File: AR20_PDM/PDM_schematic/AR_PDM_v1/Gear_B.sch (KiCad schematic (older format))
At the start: 18 parts, among them Q1 BTS50025-1TAD, U1 INA233

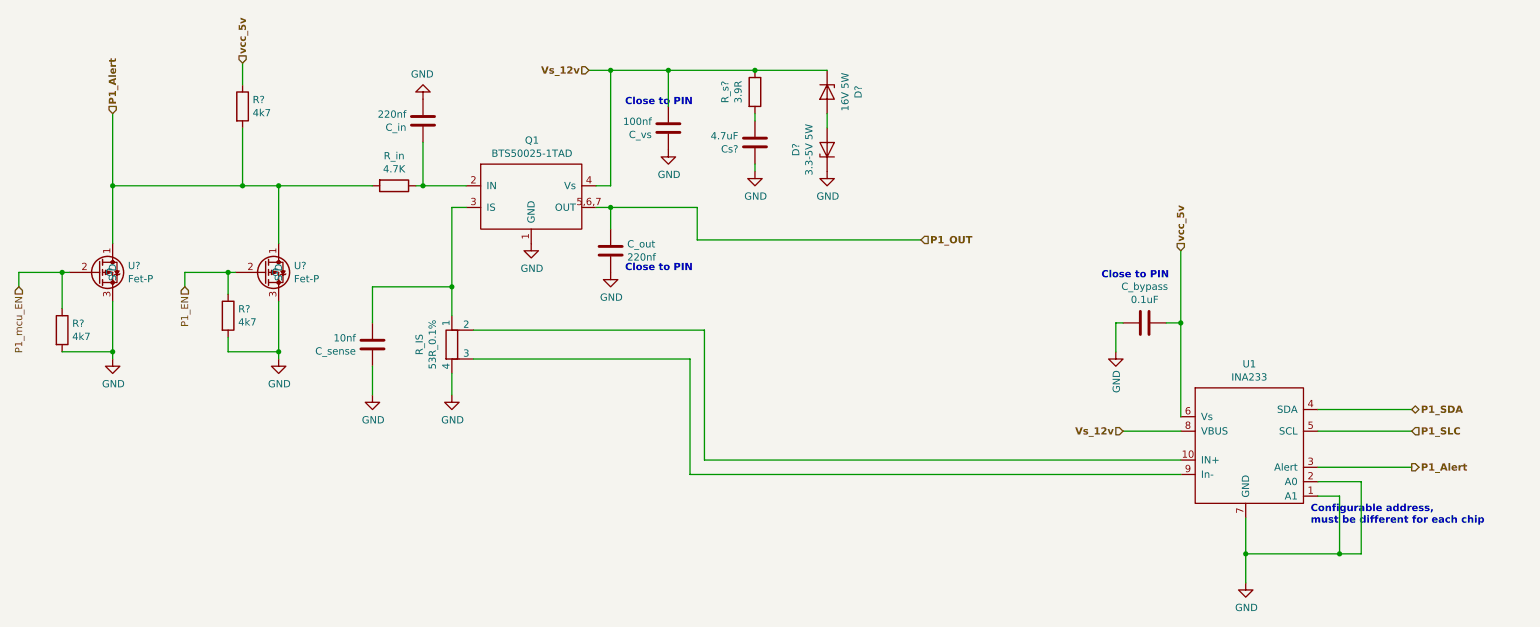
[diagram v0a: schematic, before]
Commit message: First draft of Gear phase, shutdown relays, and Direct phases.
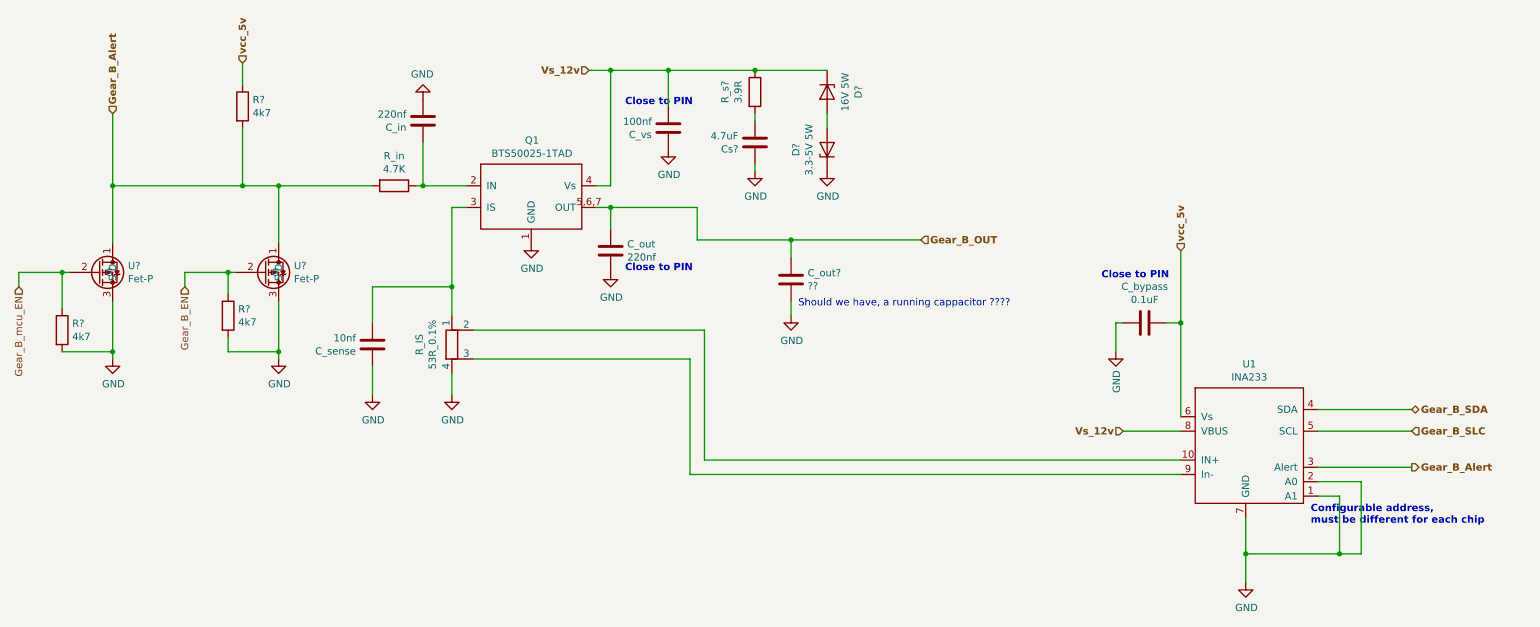
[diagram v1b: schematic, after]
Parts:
- added C_out?: ??, symbol AR20_PDM_v1-rescue:C-Device
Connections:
- net GND: now also C_out?.2
- net P1_Alert renamed Gear_B_Alert
- net P1_EN renamed Gear_B_EN
- net P1_OUT renamed Gear_B_OUT
- net Gear_B_OUT: now also C_out?.1
- net P1_SDA renamed Gear_B_SDA
- net P1_SLC renamed Gear_B_SLC
- net P1_mcu_EN renamed Gear_B_mcu_EN
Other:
- note added: "Should we have, a running cappacitor ????\n\n"
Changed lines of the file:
@@
 $Descr A4 11693 8268
 encoding utf-8
-Sheet 6 6
+Sheet 5 6
 Title ""
 Date ""
@@
 vcc_5v
 Text HLabel 10350 4350 2    50   Output ~ 10
-P1_Alert
+Gear_B_Alert
 Text HLabel 10350 3950 2    50   BiDi ~ 10
-P1_SDA
+Gear_B_SDA
 Text HLabel 10350 4100 2    50   Input ~ 10
-P1_SLC
+Gear_B_SLC
 Text Notes 4900 3000 0    50   ~ 10
 Close to PIN
@@
 	2250 1550 2250 1700
 Text HLabel 6950 2775 2    50   Input ~ 10
-P1_OUT
+Gear_B_OUT
 $Comp
 L AR20_PDM_v1-rescue:C-Device C_vs
@@
 	5350 3600 5350 4400
 Text HLabel 1350 1900 1    50   Input ~ 10
-P1_Alert
+Gear_B_Alert
 Wire Wire Line
 	9700 4350 10350 4350
@@
 Connection ~ 1000 3000
 Text HLabel 700  3100 3    50   Input ~ 0
-P1_mcu_EN
+Gear_B_mcu_EN
 Wire Wire Line
 	700  3000 700  3100
@@
 	1850 3100 1850 3000
 Text HLabel 1850 3100 3    50   Input ~ 0
-P1_EN
+Gear_B_EN
 Connection ~ 2150 3000
 Wire Wire Line
@@
 	5400 2550 5400 2775
 Wire Wire Line
-	5400 2775 6950 2775
+	5400 2775 6050 2775
 Connection ~ 4800 2550
 Wire Wire Line
@@
 Wire Wire Line
 	6300 1900 6300 2000
+$Comp
+L AR20_PDM_v1-rescue:C-Device C_out?
+U 1 1 5DEBB1FD
+P 6050 3050
+AR Path="/5DA89415/5DEBB1FD" Ref="C_out?"  Part="1"
+AR Path="/5DEB10A1/5DEBB1FD" Ref="Running_Cap?"  Part="1"
+AR Path="/5DEB20EA/5DEBB1FD" Ref="C_out?"  Part="1"
+F 0 "Running_Cap?" H 6165 3096 50  0000 L CNN
+F 1 "??" H 6165 3005 50  0000 L CNN
+F 2 "" H 6088 2900 50  0001 C CNN
+F 3 "~" H 6050 3050 50  0001 C CNN
+	1    6050 3050
+	1    0    0    -1
+$EndComp
+$Comp
+L AR20_PDM_v1-rescue:GND-power #PWR?
+U 1 1 5DEBC899
+P 6050 3300
+AR Path="/5DA89415/5DEBC899" Ref="#PWR?"  Part="1"
+AR Path="/5DEB10A1/5DEBC899" Ref="#PWR?"  Part="1"
+AR Path="/5DEB20EA/5DEBC899" Ref="#PWR?"  Part="1"
+F 0 "#PWR?" H 6050 3050 50  0001 C CNN
+F 1 "GND" H 6055 3127 50  0000 C CNN
+F 2 "" H 6050 3300 50  0001 C CNN
+F 3 "" H 6050 3300 50  0001 C CNN
+	1    6050 3300
+	1    0    0    -1
+$EndComp
+Wire Wire Line
+	6050 3300 6050 3200
+Wire Wire Line
+	6050 2900 6050 2775
+Connection ~ 6050 2775
+Wire Wire Line
+	6050 2775 6950 2775
+Text Notes 6100 3325 0    50   ~ 0
+Should we have, a running cappacitor ????\n\n
 $EndSCHEMATC

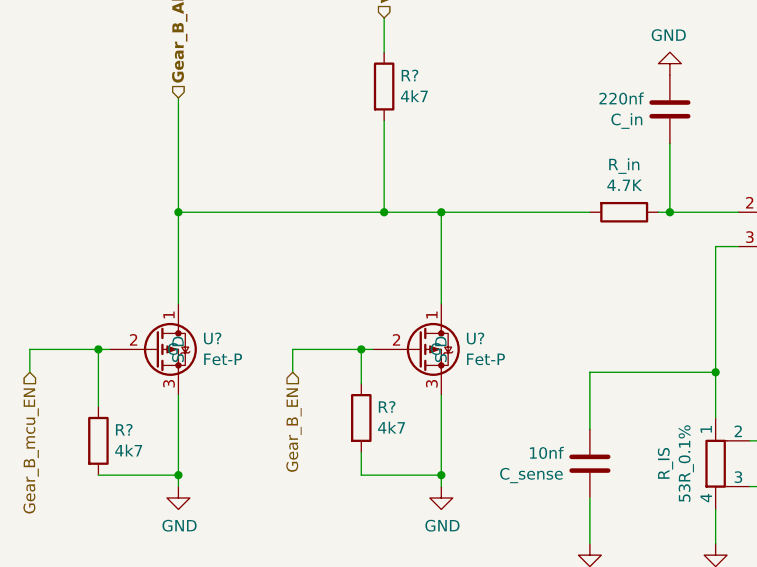
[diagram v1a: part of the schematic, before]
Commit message: Added label on mosfets, added fuel pump sinking output
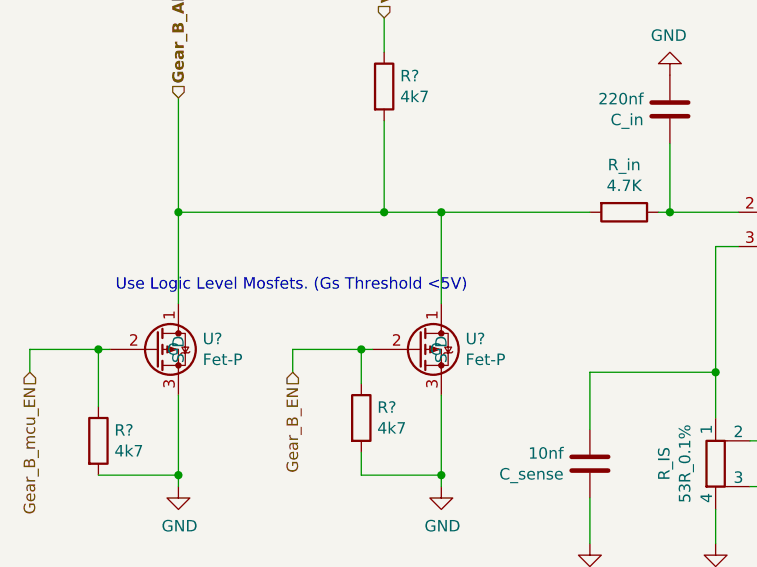
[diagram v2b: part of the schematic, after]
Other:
- note added: "Use Logic Level Mosfets. (Gs Threshold <5V)"
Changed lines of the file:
@@
 Text Notes 6100 3325 0    50   ~ 0
 Should we have, a running cappacitor ????\n\n
+Text Notes 1075 2750 0    50   ~ 0
+Use Logic Level Mosfets. (Gs Threshold <5V)
 $EndSCHEMATC
